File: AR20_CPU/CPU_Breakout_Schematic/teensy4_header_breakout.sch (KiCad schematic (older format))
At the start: 45 parts, among them J1 Conn_01x14, J2 Conn_01x14, U1 GND-1

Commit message: Edited schematic breakout teensy
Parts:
- removed J1, J2: Conn_01x14, Connector_PinHeader_2.54mm:PinHeader_1x14_P2.54mm_Vertical, symbol Connector_Generic:Conn_01x14
- removed TP? (x32): TestPoint, symbol Connector:TestPoint
- removed U1: GND-1, Teensy:Teensy40_SMT, symbol teensy4_header_breakout-rescue:Teensy4.0-Teensy
- added J1: Conn_01x05, symbol BreakoutBoardTeensy:Conn_01x05
- added J2: Teensy_pinout_02x28_Male, symbol BreakoutBoardTeensy:Teensy_pinout_02x28_Male
- added TP12, TP13, TP14, TP15, TP17, TP19: TestPoint, TestPoint:TestPoint_THTPad_D1.0mm_Drill0.5mm, symbol Connector:TestPoint
- TP1: renamed from TP?; footprint (none) -> TestPoint:TestPoint_THTPad_D1.0mm_Drill0.5mm
- gave numbers to parts that had none: 9
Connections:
- net labels added: CS_SD, MISO_SD, MOSI_SD, SCK_SD
- net labels removed: 24, 25, 26, 27, 28, 29, 30, 31, 32, 33, 3V3-1, 3V3-SD, CLK, CMD, D+, D-, DAT0, DAT1, DAT2, DAT3, GND-1, GND-SD, GNDPWR, PROGRAM, VUSB
- wire segments 73 -> 48
- no-connect marks 15 -> 1
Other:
- moved on the sheet: BT1, J3, SW1, TP1

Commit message: Added footprint to connectors
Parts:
- removed J2: Teensy_pinout_02x28_Male, symbol BreakoutBoardTeensy:Teensy_pinout_02x28_Male
- added J2: Conn_01x14, Connector_PinHeader_1.00mm:PinHeader_1x14_P1.00mm_Vertical, symbol conn_01x14:Conn_01x14
- added J4: Conn_01x14, Connector_PinHeader_1.00mm:PinHeader_1x14_P1.00mm_Vertical, symbol conn_01x14_left_teensy:Conn_01x14
- J1: footprint (none) -> Connector_PinHeader_1.00mm:PinHeader_1x05_P1.00mm_Vertical
- JP1: footprint (none) -> Jumper:SolderJumper-2_P1.3mm_Open_RoundedPad1.0x1.5mm
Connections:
- wire segments 48 -> 55
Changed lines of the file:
@@
 F 0 "JP1" V 5900 7300 50  0000 L CNN
 F 1 "SolderJumper_2_Open" V 6000 7300 50  0000 L CNN
-F 2 "" H 6000 7200 50  0001 C CNN
+F 2 "Jumper:SolderJumper-2_P1.3mm_Open_RoundedPad1.0x1.5mm" H 6000 7200 50  0001 C CNN
 F 3 "~" H 6000 7200 50  0001 C CNN
 	1    6000 7200
@@
 Text GLabel 8100 3100 0    50   Input ~ 0
 CS_SD
-Text GLabel 5650 1250 0    50   Input ~ 0
-CS_SD
 $Bitmap
 Pos 1650 1500
@@
 $EndBitmap
 $Comp
-L BreakoutBoardTeensy:Teensy_pinout_02x28_Male J2
-U 1 1 5DEF51B6
-P 3550 4000
-F 0 "J2" H 3492 4781 50  0000 C CNN
-F 1 "Teensy_pinout_02x28_Male" H 3492 4690 50  0000 C CNN
-F 2 "" H 3550 4000 50  0001 C CNN
-F 3 "~" H 3550 4000 50  0001 C CNN
-	1    3550 4000
-	1    0    0    -1
-$EndComp
-$Comp
 L BreakoutBoardTeensy:Conn_01x05 J1
 U 1 1 5DF02C06
@@
 F 0 "J1" V 3364 4512 50  0000 R CNN
 F 1 "Conn_01x05" V 3273 4512 50  0000 R CNN
-F 2 "" H 3400 4800 50  0001 C CNN
+F 2 "Connector_PinHeader_1.00mm:PinHeader_1x05_P1.00mm_Vertical" H 3400 4800 50  0001 C CNN
 F 3 "~" H 3400 4800 50  0001 C CNN
 	1    3400 4800
@@
 	3650 5400 3650 5000
 Wire Wire Line
-	4150 4700 3750 4700
+	4150 4700 3800 4700
+Wire Wire Line
+	3750 3800 3800 3800
+Wire Wire Line
+	4150 3700 3800 3700
+Wire Wire Line
+	4150 3400 3800 3400
+Wire Wire Line
+	4150 3500 3800 3500
+$Comp
+L conn_01x14_left_teensy:Conn_01x14 J4
+U 1 1 5DDC81B7
+P 3700 4000
+F 0 "J4" H 3682 4817 50  0000 C CNN
+F 1 "Conn_01x14" H 3682 4726 50  0000 C CNN
+F 2 "Connector_PinHeader_1.00mm:PinHeader_1x14_P1.00mm_Vertical" H 3600 3900 50  0001 C CNN
+F 3 "~" H 3600 3900 50  0001 C CNN
+	1    3700 4000
+	1    0    0    -1
+$EndComp
+$Comp
+L conn_01x14:Conn_01x14 J2
+U 1 1 5DDC932D
+P 3200 4000
+F 0 "J2" H 3280 3992 50  0000 L CNN
+F 1 "Conn_01x14" H 3280 3901 50  0000 L CNN
+F 2 "Connector_PinHeader_1.00mm:PinHeader_1x14_P1.00mm_Vertical" H 3200 4000 50  0001 C CNN
+F 3 "~" H 3200 4000 50  0001 C CNN
+	1    3200 4000
+	1    0    0    -1
+$EndComp
+Connection ~ 3800 4700
+Wire Wire Line
+	3800 4700 3750 4700
+Connection ~ 3800 3800
+Wire Wire Line
+	3800 3800 4150 3800
+Connection ~ 3800 3700
+Wire Wire Line
+	3800 3700 3750 3700
+Connection ~ 3800 3500
 Wire Wire Line
-	3750 3800 4150 3800
+	3800 3500 3750 3500
+Connection ~ 3800 3400
 Wire Wire Line
-	4150 3700 3750 3700
+	3800 3400 3750 3400
 $EndSCHEMATC

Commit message: Edited test points
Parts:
- added TP10, TP11, TP16, TP18, TP2, TP20, TP21, TP22, TP3, TP4, TP5, TP6, TP7, TP8, TP9: TestPoint, TestPoint:TestPoint_THTPad_D1.0mm_Drill0.5mm, symbol Connector:TestPoint
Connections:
- wire segments 55 -> 53
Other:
- moved on the sheet: TP12, TP13, TP14

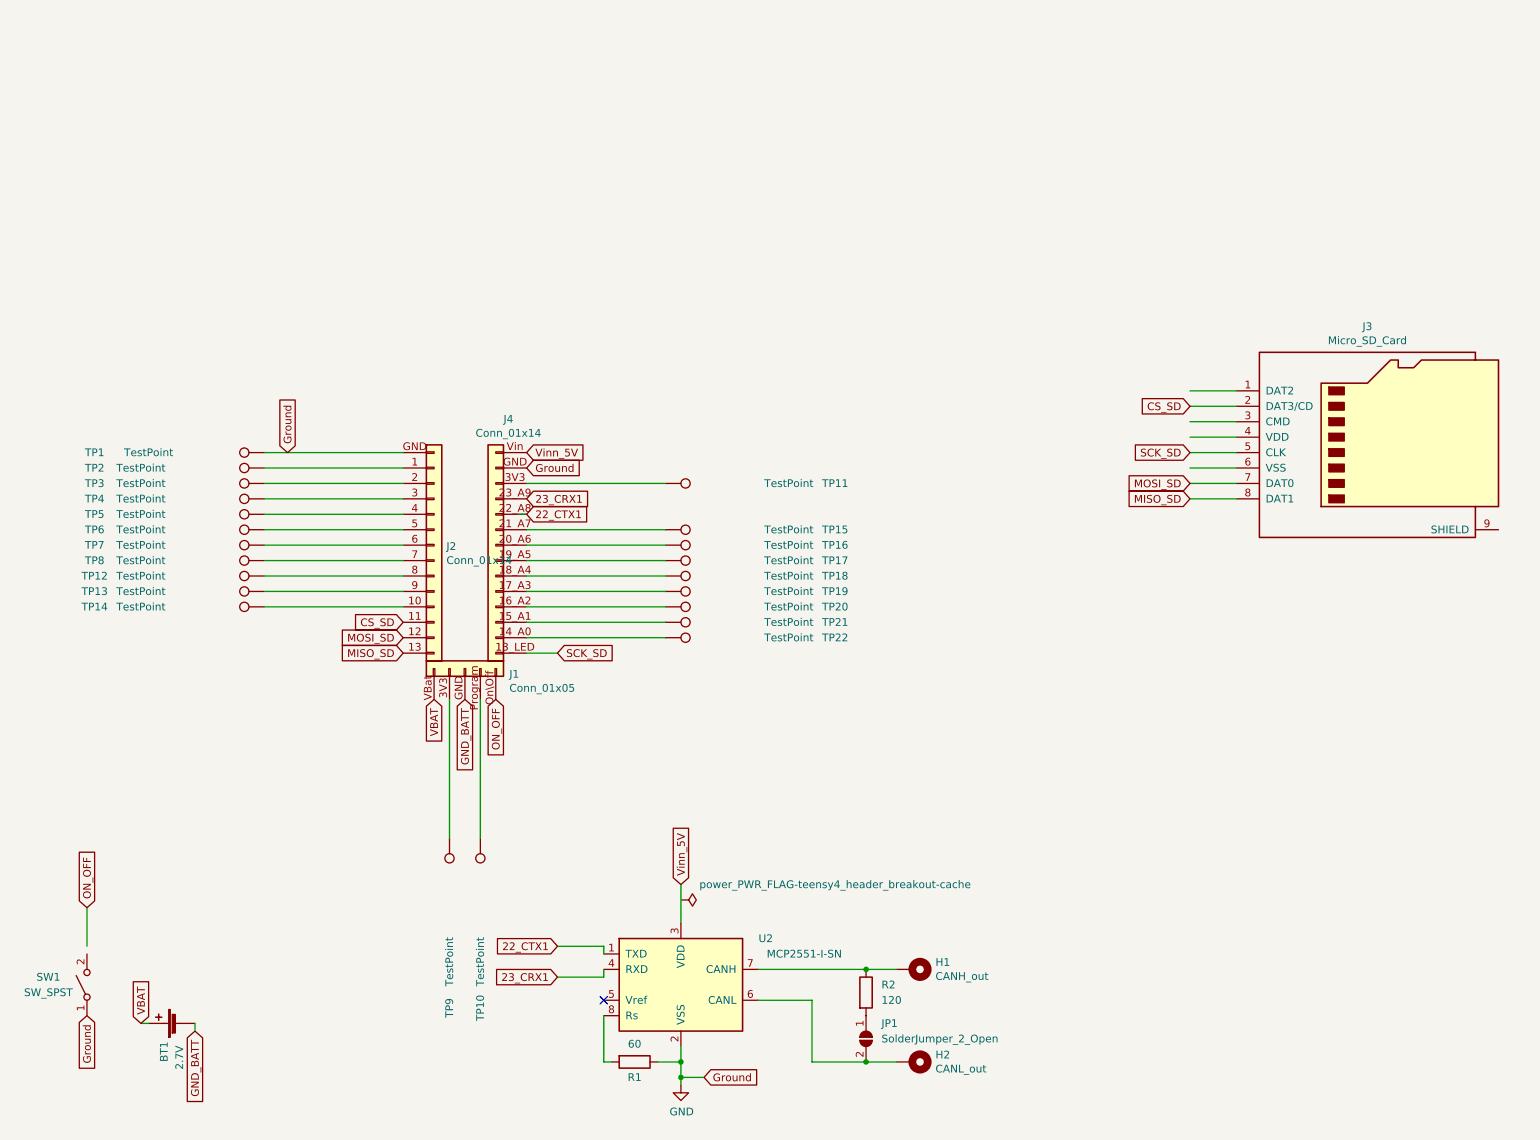
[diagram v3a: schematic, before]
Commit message: ADDED NEW FOOTPRINT TO TEENSY CONNECTORS
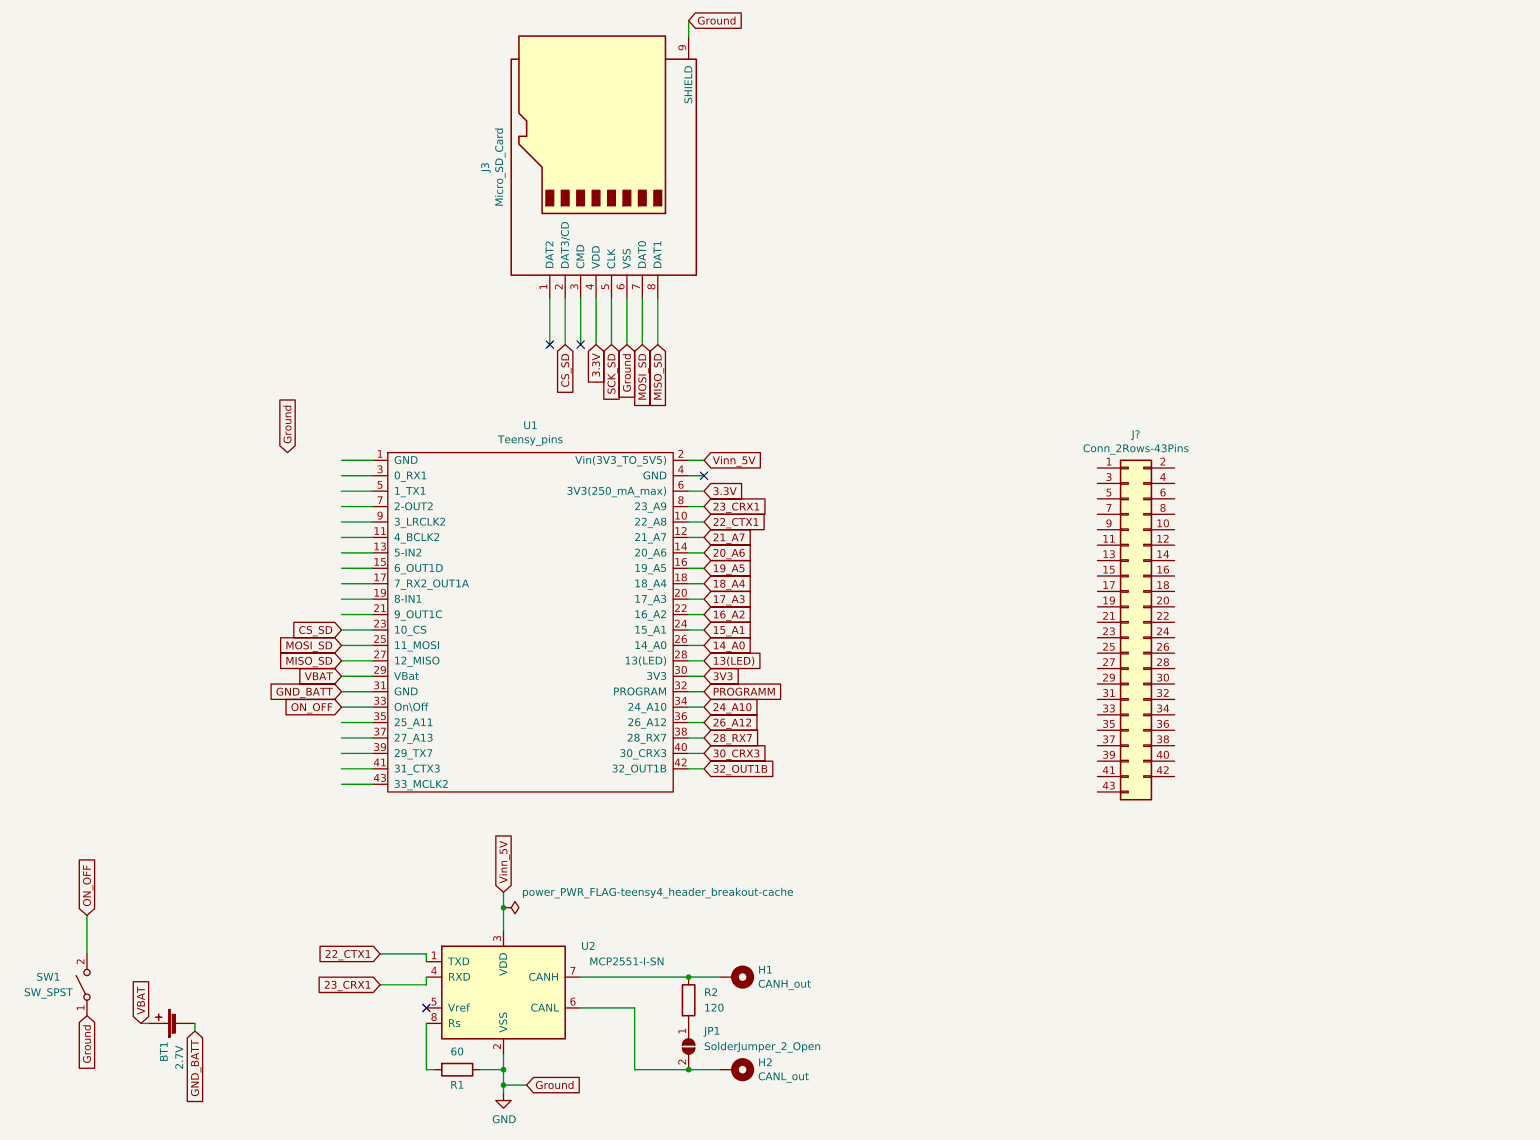
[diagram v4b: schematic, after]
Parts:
- removed J1: Conn_01x05, Connector_PinHeader_1.00mm:PinHeader_1x05_P1.00mm_Vertical, symbol BreakoutBoardTeensy:Conn_01x05
- removed J2: Conn_01x14, Connector_PinHeader_1.00mm:PinHeader_1x14_P1.00mm_Vertical, symbol conn_01x14:Conn_01x14
- removed J4: Conn_01x14, Connector_PinHeader_1.00mm:PinHeader_1x14_P1.00mm_Vertical, symbol conn_01x14_left_teensy:Conn_01x14
- removed TP1, TP10, TP11, TP12, TP13, TP14, TP15, TP16, TP17, TP18, TP19, TP2, TP20, TP21, TP22, TP3, TP4, TP5, TP6, TP7, TP8, TP9: TestPoint, TestPoint:TestPoint_THTPad_D1.0mm_Drill0.5mm, symbol Connector:TestPoint
- added J?: Conn_2Rows-43Pins, symbol Connector_Generic:Conn_2Rows-43Pins
- added U1: Teensy_pins, Teensy_Footprint_Library:Teensy_40_footprint, symbol BreakoutBoardTeensy:Teensy_pins
- H1, H2: footprint (none) -> TestPoint:TestPoint_THTPad_D1.0mm_Drill0.5mm
- J3: footprint (none) -> Connector_Card:microSD_HC_Hirose_DM3D-SF
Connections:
- net labels added: 13(LED), 14_A0, 15_A1, 16_A2, 17_A3, 18_A4, 19_A5, 20_A6, 21_A7, 24_A10, 26_A12, 28_RX7, 3.3V, 30_CRX3, 32_OUT1B, 3V3, PROGRAMM
- wire segments 53 -> 74
- no-connect marks 1 -> 4
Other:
- moved on the sheet: H1, H2, J3, JP1, R1, R2, U2
